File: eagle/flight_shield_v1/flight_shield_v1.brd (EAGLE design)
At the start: 101.3 x 78.7 mm, 16 parts

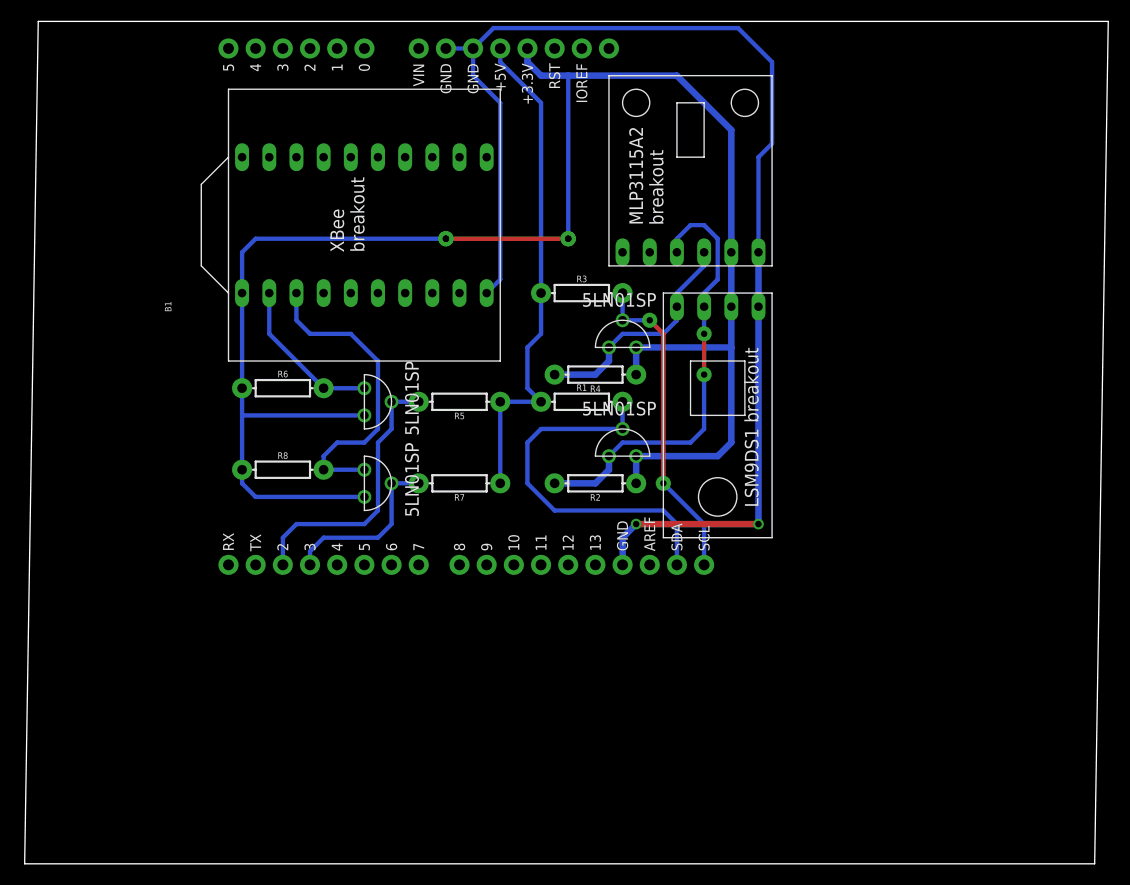
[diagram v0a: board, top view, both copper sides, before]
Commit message: IMU / AHRS prosessering begynner å bli bedre. Flyttet arduino filer til git.
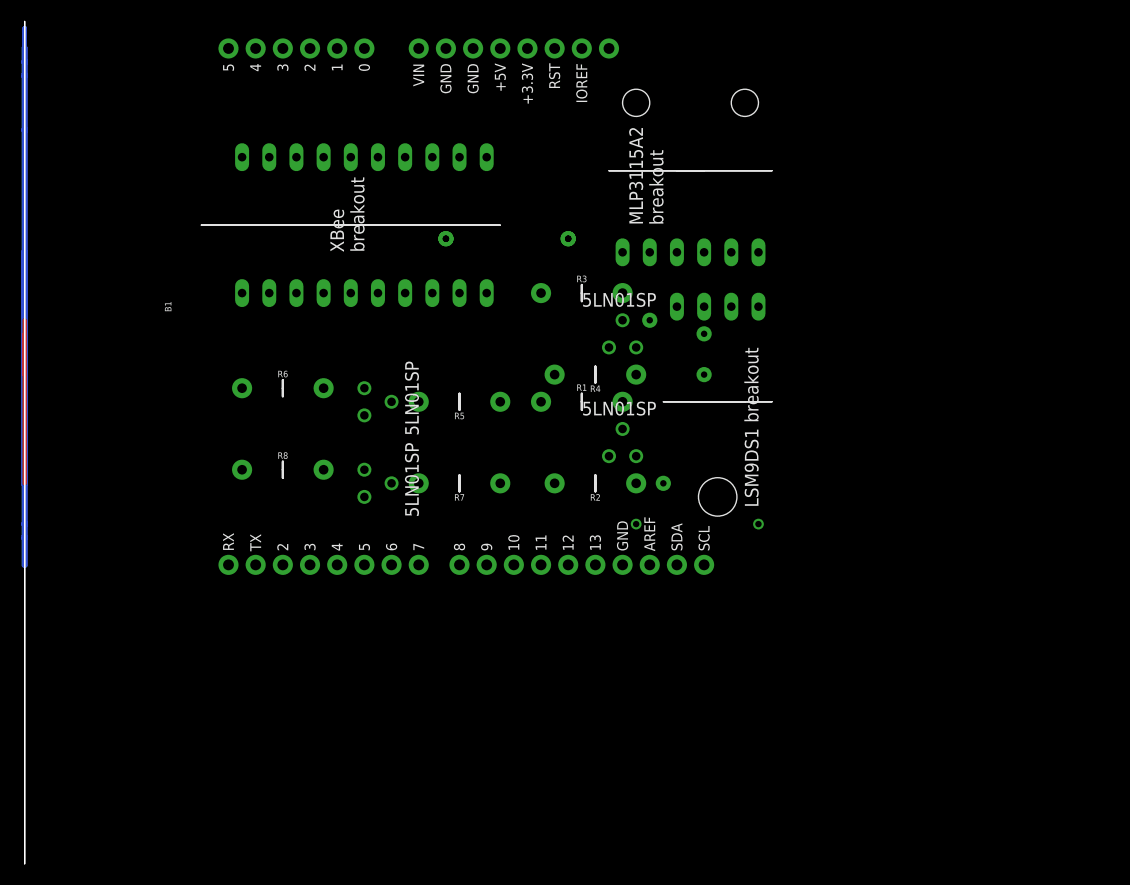
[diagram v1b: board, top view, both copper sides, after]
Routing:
- net N$6: track 166.8 -> 82.5 mm
- net N$3: track 116.5 -> 74.9 mm
- net N$7: track 35.1 -> 15.2 mm
- net N$8: track 41.3 -> 26.7 mm
- net N$13: track 29.3 -> 16.5 mm
- net N$12: track 25.7 -> 15.2 mm
- net N$9: track 21.7 -> 11.4 mm
- net N$14: track 16.3 -> 7.62 mm
- net N$15: track 47.1 -> 40.6 mm
- net N$11: track 14.8 -> 8.89 mm
- net N$10: track 30.0 -> 25.4 mm
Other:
- board outline removed
